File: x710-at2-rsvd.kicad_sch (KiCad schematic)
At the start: 37 parts, among them J5 PinHeader_1x3_P2.54mm_Drill1.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, U4 EZX710AT2_S_LMR5

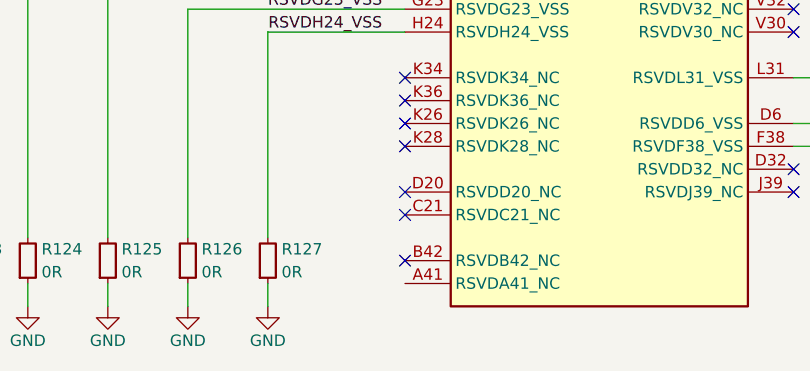
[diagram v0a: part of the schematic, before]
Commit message: [#85196] Clear ERC, minor schematic fixes
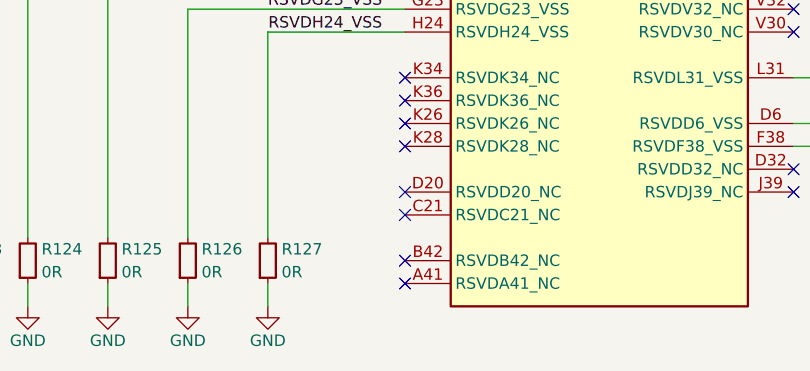
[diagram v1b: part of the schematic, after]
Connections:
- no-connect marks 64 -> 65
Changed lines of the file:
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@@
+	)
+	(no_connect
+		(at 195.58 247.65)
 	)
 	(no_connect

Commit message: [#85196] Re-annotate schematic
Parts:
- renumbered J5 to J8, R97 to R128, R98 to R129, R99 to R130, R100 to R131, R101 to R132, R102 to R133, R103 to R134, R104 to R135, R105 to R136, R106 to R137, R107 to R138, R108 to R139, R109 to R140, R110 to R141, R111 to R142, R112 to R143, R113 to R144, R114 to R145, R115 to R146, R116 to R147, R117 to R148, R118 to R149, R119 to R150, R120 to R151, R121 to R152, R122 to R153, R123 to R154, R124 to R155, R125 to R156, R126 to R157, R127 to R158, R128 to R159, R129 to R160, R130 to R161, U4 to U9
